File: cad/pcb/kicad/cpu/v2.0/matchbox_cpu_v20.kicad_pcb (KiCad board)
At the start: 6 copper layers, 40 x 66 mm, 64 parts, among them CN1 ?M02B-SRSS-TBS, P1 DF12-32-DP, P2 DF12-32-DP, P3 DF12-32-DP, P4 DF12-32-DP, Q1 FDN360P, Q2 FDN360P, SW1 B3U-3100PM-B, SW2 B3U-3100PM-B, U2 MCP1703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

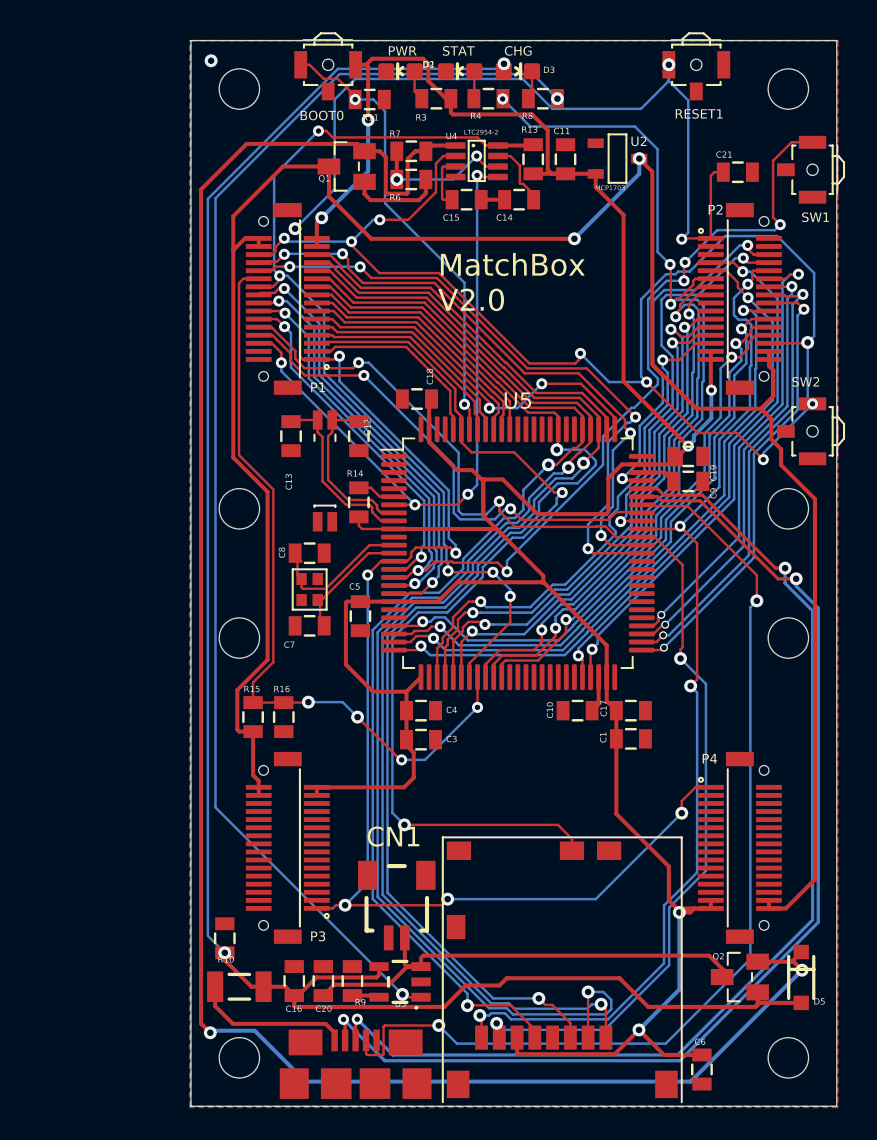
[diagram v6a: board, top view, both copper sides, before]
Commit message: Improve ground fill polygons.
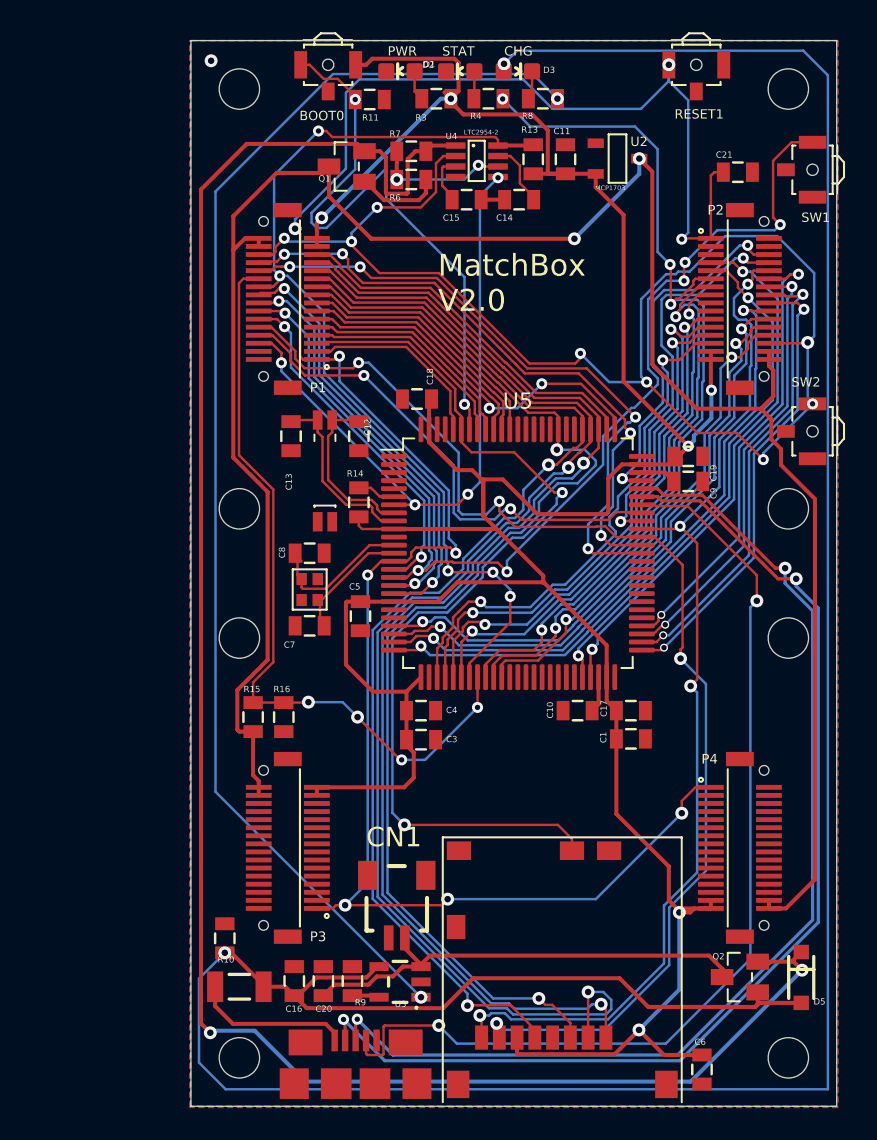
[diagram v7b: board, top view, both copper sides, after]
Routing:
- net /VCC_USBF: track 116.0 -> 177.1 mm
- net /BOOT0: track 28.8 -> 38.1 mm
- net /VCC_3V3: track 189.0 -> 191.0 mm
- net /PC13: track 40.7 -> 39.8 mm
- net /VBAT: track 29.9 -> 29.2 mm
- net Net-(R6-Pad2): track 8.94 -> 8.41 mm

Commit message: Clean up CPUv2 component labels
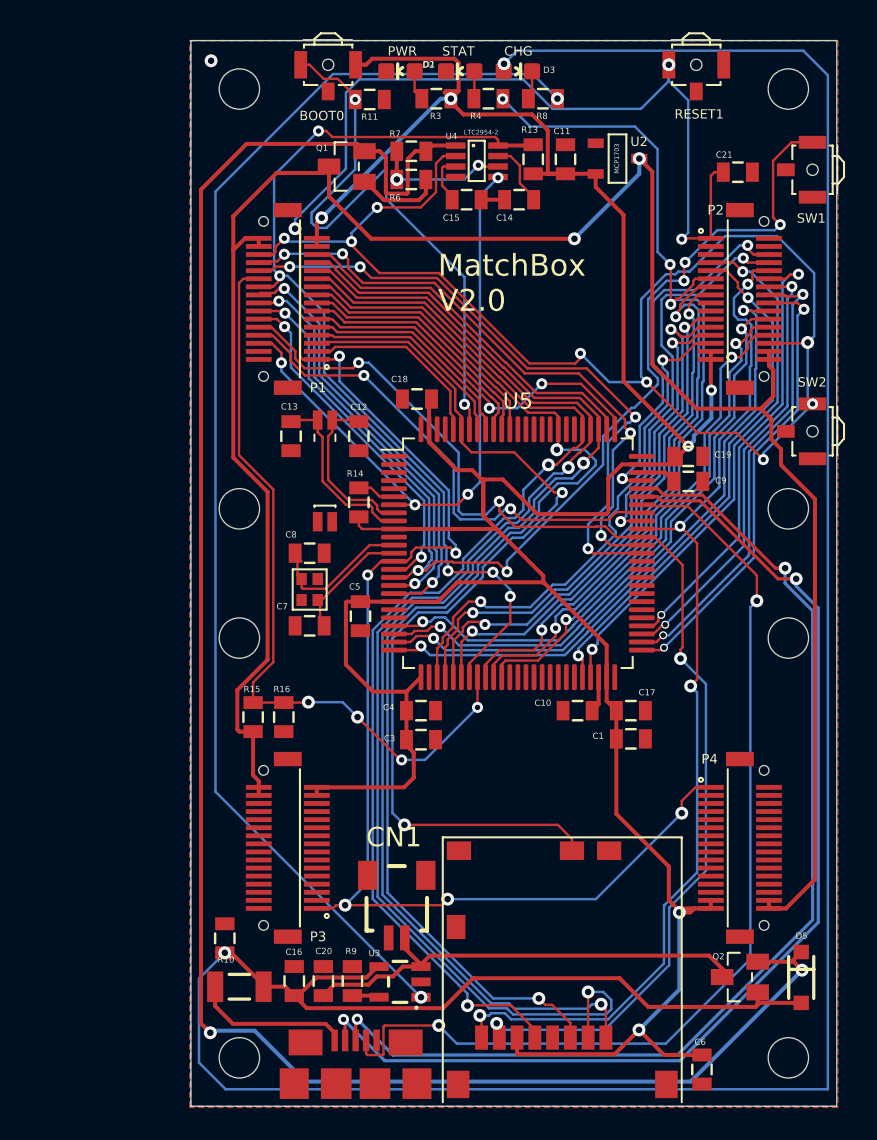
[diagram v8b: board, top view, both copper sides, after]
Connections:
- RESET1 pad GND: GND -> Net-(RESET1-PadGND)
